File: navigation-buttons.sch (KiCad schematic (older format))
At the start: 26 parts

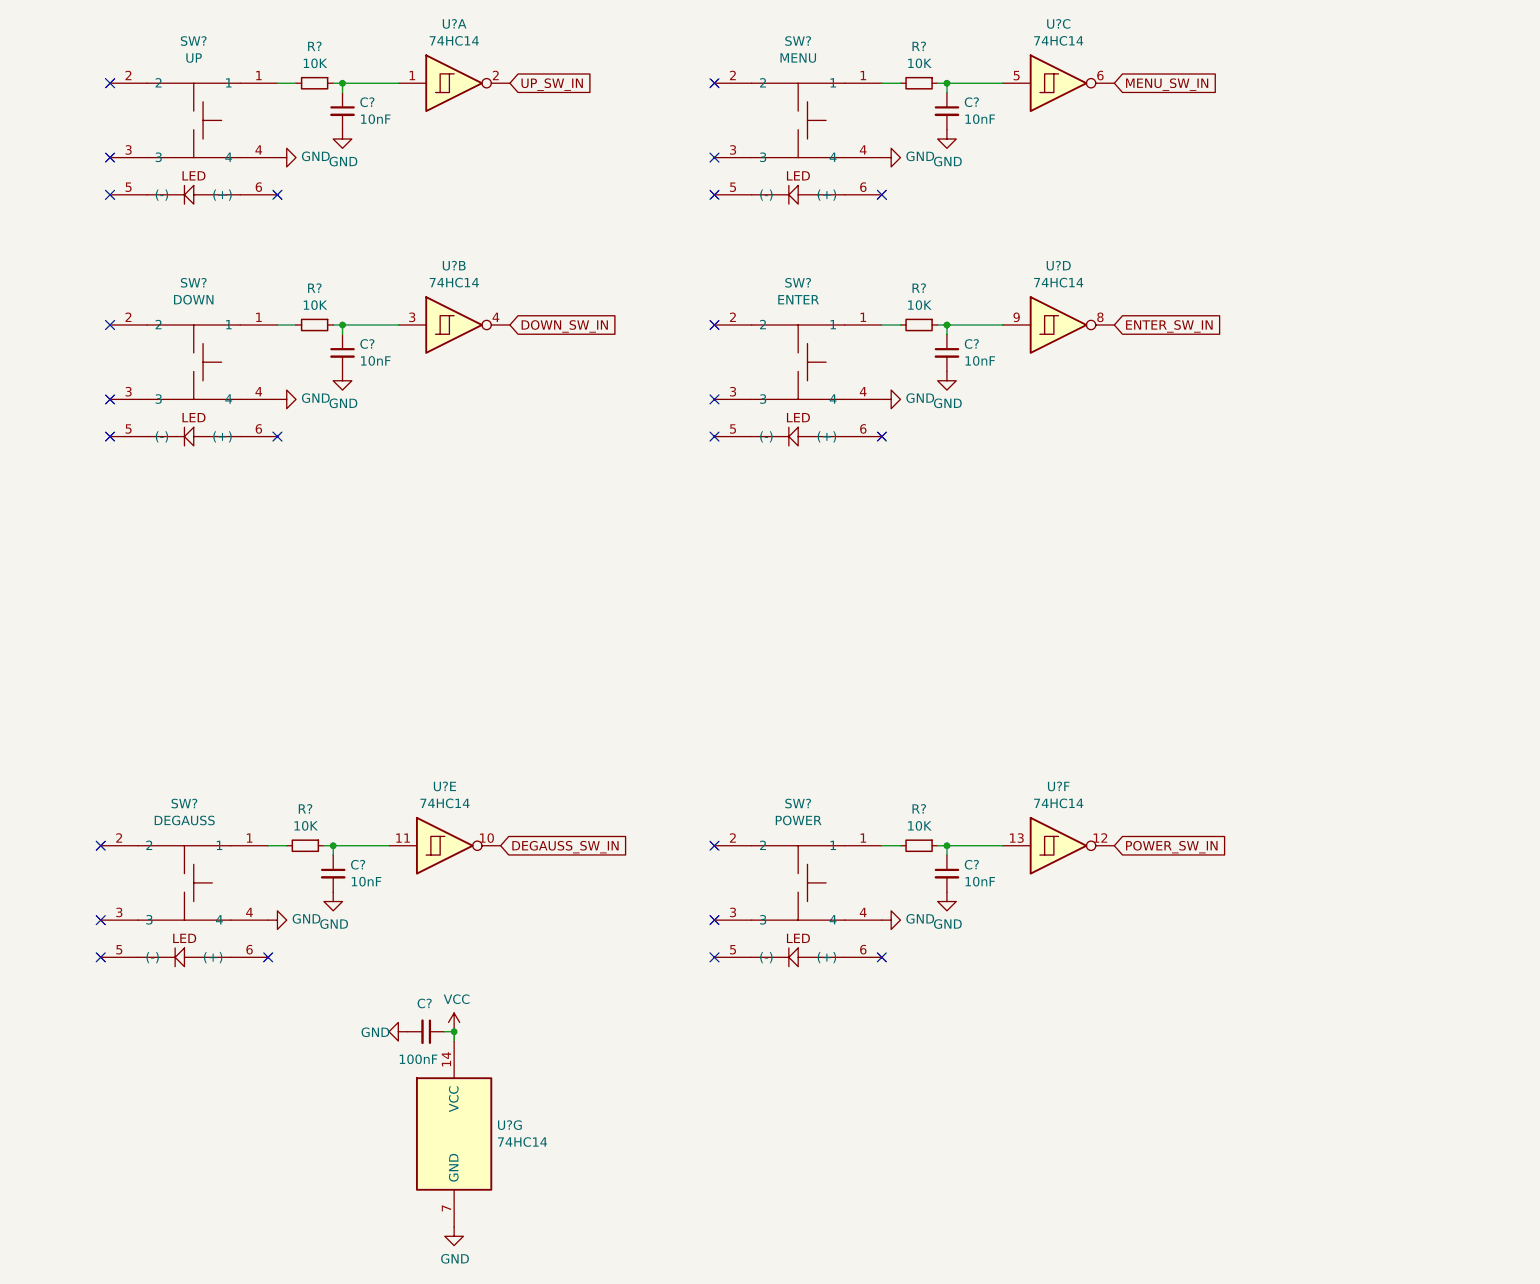
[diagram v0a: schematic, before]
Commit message: Initial PCB routed
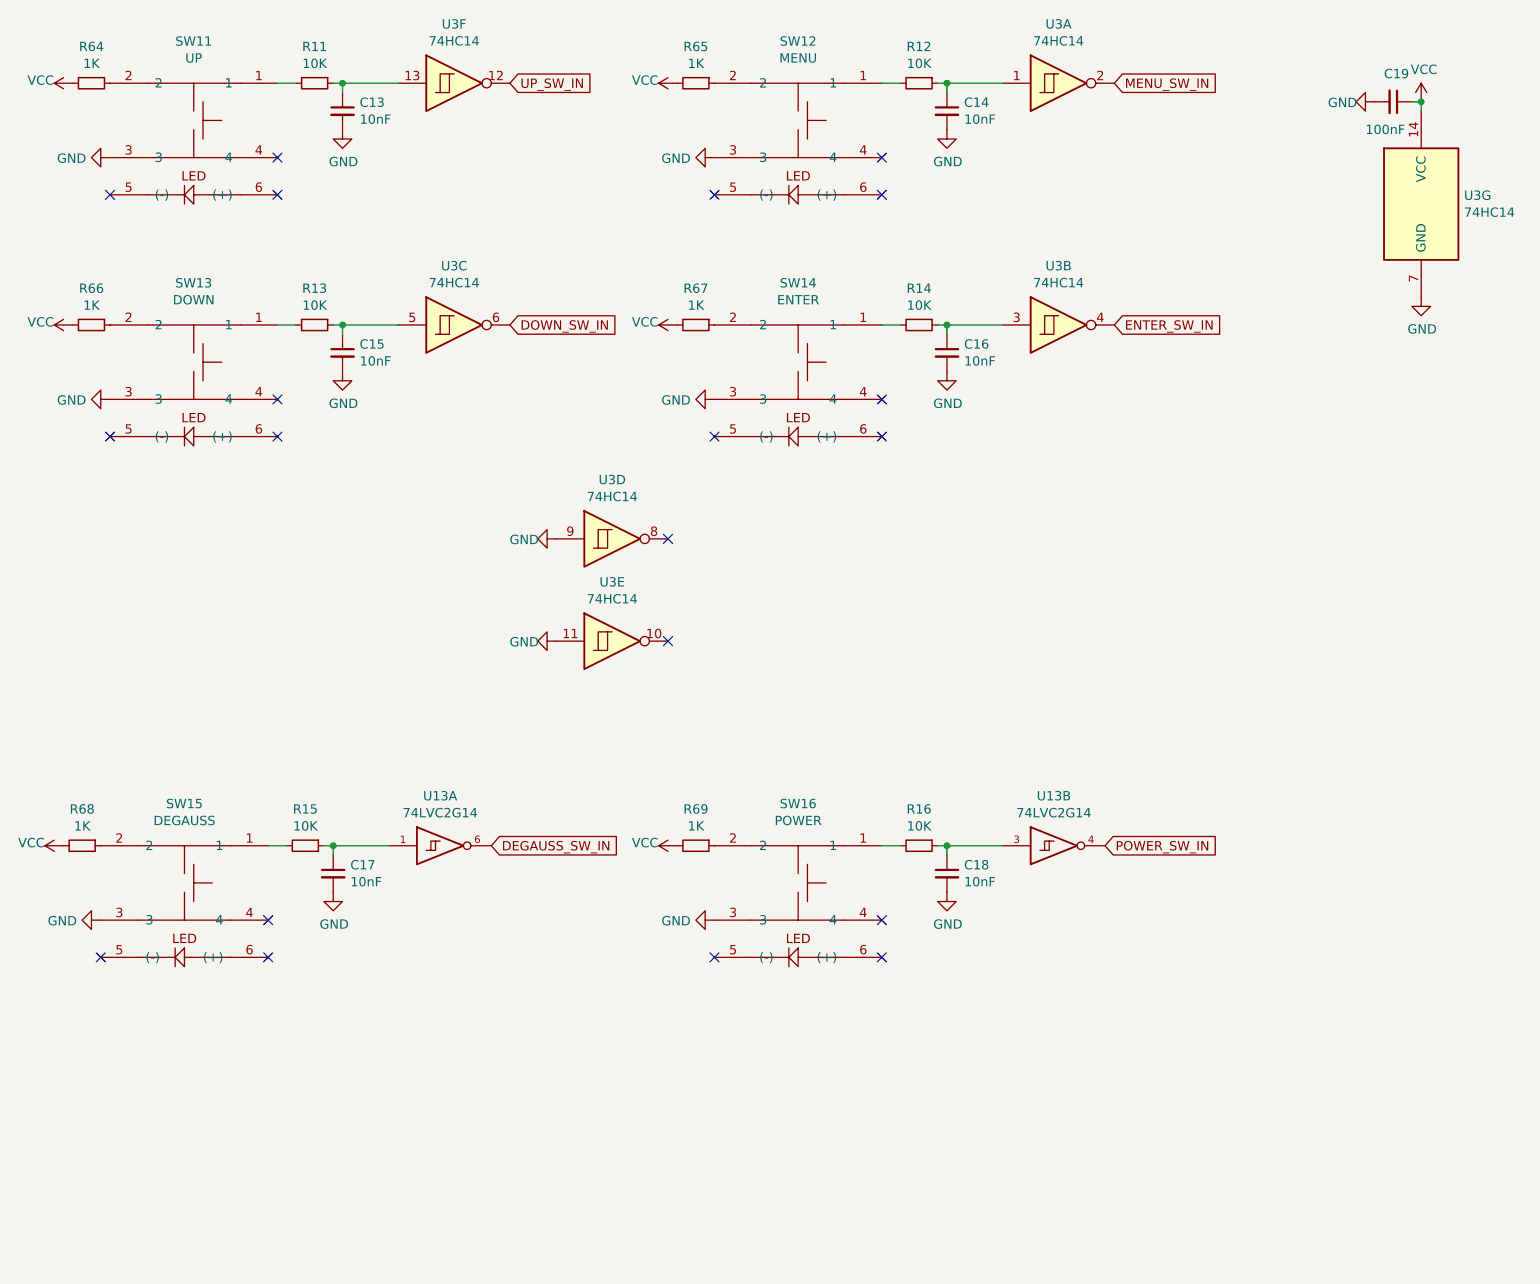
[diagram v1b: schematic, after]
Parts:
- removed U? (x2): 74HC14, symbol 74xx:74HC14
- added R64, R65, R66, R67, R68, R69: 1K, Resistor_SMD:R_0603_1608Metric_Pad0.98x0.95mm_HandSolder, symbol Device:R_Small
- added U13: 74LVC2G14, Package_TO_SOT_SMD:SOT-23-6_Handsoldering, symbol 74xGxx:74LVC2G14
- added unit 6 of U3
- added unit 5 of U3
- C13, C14, C15, C16, C17, C18, C19: renamed from C?; footprint (none) -> Capacitor_SMD:C_0603_1608Metric_Pad1.08x0.95mm_HandSolder
- R11, R12, R13, R14, R15, R16: renamed from R?; footprint (none) -> Resistor_SMD:R_0603_1608Metric_Pad0.98x0.95mm_HandSolder
- SW11, SW12, SW13, SW14, SW15, SW16: renamed from SW?; footprint (none) -> TL-1240:TL-1240
- U3: renamed from U?; footprint (none) -> Package_SO:SSOP-14_5.3x6.2mm_P0.65mm
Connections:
- net DEGAUSS_SW_IN: now also U13.6
- net DOWN_SW_IN: now also U3.6; no longer U3.4
- net ENTER_SW_IN: now also U3.4; no longer U3.8
- net GND: now also SW11.3, SW12.3, SW13.3, SW14.3, SW15.3, SW16.3, U3.9, U13.2 (GND), U13.2 (GND), U3.11; no longer SW11.4, SW12.4, SW13.4, SW14.4, SW15.4, SW16.4
- net MENU_SW_IN: now also U3.2; no longer U3.6
- net POWER_SW_IN: now also U13.4
- net UP_SW_IN: now also U3.12; no longer U3.2
- net VCC: now also R64.2, R65.2, R66.2, R67.2, R68.2, R69.2, U13.5 (VCC), U13.5 (VCC)
- net at SW11.2: now also R64.1
- net at C13.1, R11.1: now also U3.13; no longer U3.1
- net at SW13.2: now also R66.1
- net at C15.1, R13.1: now also U3.5; no longer U3.3
- net at SW12.2: now also R65.1
- net at C14.1, R12.1: now also U3.1; no longer U3.5
- net at SW14.2: now also R67.1
- net at C16.1, R14.1: now also U3.3; no longer U3.9
- net at SW15.2: now also R68.1
- net at C17.1, R15.1: now also U13.1
- net at SW16.2: now also R69.1
- net at C18.1, R16.1: now also U13.3
- no-connect marks 24 -> 20
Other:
- moved on the sheet: C19, U3A, U3B, U3C, U3D, U3G

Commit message: Initial revision B
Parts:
- SW11, SW12, SW13, SW14, SW15, SW16: footprint TL-1240:TL-1240 -> TL-1265:TL-1265_NO_LED; symbol e-switch-tact:TL-1240 -> e-switch-tact:TL-1240-NO_LED
- U3: footprint Package_SO:SSOP-14_5.3x6.2mm_P0.65mm -> Package_SO:TSSOP-14_4.4x5mm_P0.65mm
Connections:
- no-connect marks 20 -> 8
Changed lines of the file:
@@
 $EndDescr
 $Comp
-L e-switch-tact:TL-1240 SW13
+L e-switch-tact:TL-1240-NO_LED SW13
 U 1 1 61AC16B9
-P 1450 2650
-F 0 "SW13" H 1450 3125 50  0000 C CNN
-F 1 "DOWN" H 1450 3034 50  0000 C CNN
-F 2 "TL-1240:TL-1240" H 1450 2800 50  0001 C CNN
-F 3 "" H 1450 2800 50  0001 C CNN
-	1    1450 2650
-	1    0    0    -1
-$EndComp
-NoConn ~ 1000 3000
-NoConn ~ 1900 3000
+P 1450 2600
+F 0 "SW13" H 1450 3075 50  0000 C CNN
+F 1 "DOWN" H 1450 2984 50  0000 C CNN
+F 2 "TL-1265:TL-1265_NO_LED" H 1450 2750 50  0001 C CNN
+F 3 "" H 1450 2750 50  0001 C CNN
+	1    1450 2600
+	1    0    0    -1
+$EndComp
 NoConn ~ 1900 2800
 $Comp
@@
 $EndComp
 NoConn ~ 1900 1500
-NoConn ~ 1900 1700
-NoConn ~ 1000 1700
-$Comp
-L e-switch-tact:TL-1240 SW11
+$Comp
+L e-switch-tact:TL-1240-NO_LED SW11
 U 1 1 61AB54CB
-P 1450 1350
-F 0 "SW11" H 1450 1825 50  0000 C CNN
-F 1 "UP" H 1450 1734 50  0000 C CNN
-F 2 "TL-1240:TL-1240" H 1450 1500 50  0001 C CNN
-F 3 "" H 1450 1500 50  0001 C CNN
-	1    1450 1350
-	1    0    0    -1
-$EndComp
-$Comp
-L e-switch-tact:TL-1240 SW12
-U 1 1 61AC42D3
-P 4700 1350
-F 0 "SW12" H 4700 1825 50  0000 C CNN
-F 1 "MENU" H 4700 1734 50  0000 C CNN
-F 2 "TL-1240:TL-1240" H 4700 1500 50  0001 C CNN
-F 3 "" H 4700 1500 50  0001 C CNN
-	1    4700 1350
-	1    0    0    -1
-$EndComp
-NoConn ~ 4250 1700
-NoConn ~ 5150 1700
+P 1450 1300
+F 0 "SW11" H 1450 1775 50  0000 C CNN
+F 1 "UP" H 1450 1684 50  0000 C CNN
+F 2 "TL-1265:TL-1265_NO_LED" H 1450 1450 50  0001 C CNN
+F 3 "" H 1450 1450 50  0001 C CNN
+	1    1450 1300
+	1    0    0    -1
+$EndComp
 NoConn ~ 5150 1500
 $Comp
@@
 MENU_SW_IN
 $Comp
-L e-switch-tact:TL-1240 SW14
+L e-switch-tact:TL-1240-NO_LED SW14
 U 1 1 61AC5650
-P 4700 2650
-F 0 "SW14" H 4700 3125 50  0000 C CNN
-F 1 "ENTER" H 4700 3034 50  0000 C CNN
-F 2 "TL-1240:TL-1240" H 4700 2800 50  0001 C CNN
-F 3 "" H 4700 2800 50  0001 C CNN
-	1    4700 2650
-	1    0    0    -1
-$EndComp
-NoConn ~ 4250 3000
-NoConn ~ 5150 3000
+P 4700 2600
+F 0 "SW14" H 4700 3075 50  0000 C CNN
+F 1 "ENTER" H 4700 2984 50  0000 C CNN
+F 2 "TL-1265:TL-1265_NO_LED" H 4700 2750 50  0001 C CNN
+F 3 "" H 4700 2750 50  0001 C CNN
+	1    4700 2600
+	1    0    0    -1
+$EndComp
 NoConn ~ 5150 2800
 $Comp
@@
 ENTER_SW_IN
 $Comp
-L e-switch-tact:TL-1240 SW15
+L e-switch-tact:TL-1240-NO_LED SW15
 U 1 1 61ACA481
-P 1400 5450
-F 0 "SW15" H 1400 5925 50  0000 C CNN
-F 1 "DEGAUSS" H 1400 5834 50  0000 C CNN
-F 2 "TL-1240:TL-1240" H 1400 5600 50  0001 C CNN
-F 3 "" H 1400 5600 50  0001 C CNN
-	1    1400 5450
-	1    0    0    -1
-$EndComp
-NoConn ~ 950  5800
-NoConn ~ 1850 5800
+P 1400 5400
+F 0 "SW15" H 1400 5875 50  0000 C CNN
+F 1 "DEGAUSS" H 1400 5784 50  0000 C CNN
+F 2 "TL-1265:TL-1265_NO_LED" H 1400 5550 50  0001 C CNN
+F 3 "" H 1400 5550 50  0001 C CNN
+	1    1400 5400
+	1    0    0    -1
+$EndComp
 NoConn ~ 1850 5600
 $Comp
@@
 DEGAUSS_SW_IN
 $Comp
-L e-switch-tact:TL-1240 SW16
+L e-switch-tact:TL-1240-NO_LED SW16
 U 1 1 61AD8CF5
-P 4700 5450
-F 0 "SW16" H 4700 5925 50  0000 C CNN
-F 1 "POWER" H 4700 5834 50  0000 C CNN
-F 2 "TL-1240:TL-1240" H 4700 5600 50  0001 C CNN
-F 3 "" H 4700 5600 50  0001 C CNN
-	1    4700 5450
-	1    0    0    -1
-$EndComp
-NoConn ~ 4250 5800
-NoConn ~ 5150 5800
+P 4700 5400
+F 0 "SW16" H 4700 5875 50  0000 C CNN
+F 1 "POWER" H 4700 5784 50  0000 C CNN
+F 2 "TL-1265:TL-1265_NO_LED" H 4700 5550 50  0001 C CNN
+F 3 "" H 4700 5550 50  0001 C CNN
+	1    4700 5400
+	1    0    0    -1
+$EndComp
 NoConn ~ 5150 5600
 $Comp
@@
 F 0 "U3" H 6100 1417 50  0000 C CNN
 F 1 "74HC14" H 6100 1326 50  0000 C CNN
-F 2 "Package_SO:SSOP-14_5.3x6.2mm_P0.65mm" H 6100 1100 50  0001 C CNN
+F 2 "Package_SO:TSSOP-14_4.4x5mm_P0.65mm" H 6100 1100 50  0001 C CNN
 F 3 "http://www.ti.com/lit/gpn/sn74HC14" H 6100 1100 50  0001 C CNN
 	1    6100 1100
@@
 F 0 "U3" H 6100 2717 50  0000 C CNN
 F 1 "74HC14" H 6100 2626 50  0000 C CNN
-F 2 "Package_SO:SSOP-14_5.3x6.2mm_P0.65mm" H 6100 2400 50  0001 C CNN
+F 2 "Package_SO:TSSOP-14_4.4x5mm_P0.65mm" H 6100 2400 50  0001 C CNN
 F 3 "http://www.ti.com/lit/gpn/sn74HC14" H 6100 2400 50  0001 C CNN
 	2    6100 2400
@@
 F 0 "U3" H 3700 3867 50  0000 C CNN
 F 1 "74HC14" H 3700 3776 50  0000 C CNN
-F 2 "Package_SO:SSOP-14_5.3x6.2mm_P0.65mm" H 3700 3550 50  0001 C CNN
+F 2 "Package_SO:TSSOP-14_4.4x5mm_P0.65mm" H 3700 3550 50  0001 C CNN
 F 3 "http://www.ti.com/lit/gpn/sn74HC14" H 3700 3550 50  0001 C CNN
 	4    3700 3550
@@
 F 0 "U3" H 2850 2717 50  0000 C CNN
 F 1 "74HC14" H 2850 2626 50  0000 C CNN
-F 2 "Package_SO:SSOP-14_5.3x6.2mm_P0.65mm" H 2850 2400 50  0001 C CNN
+F 2 "Package_SO:TSSOP-14_4.4x5mm_P0.65mm" H 2850 2400 50  0001 C CNN
 F 3 "http://www.ti.com/lit/gpn/sn74HC14" H 2850 2400 50  0001 C CNN
 	3    2850 2400
@@
 F 0 "U3" H 8280 1796 50  0000 L CNN
 F 1 "74HC14" H 8280 1705 50  0000 L CNN
-F 2 "Package_SO:SSOP-14_5.3x6.2mm_P0.65mm" H 8050 1750 50  0001 C CNN
+F 2 "Package_SO:TSSOP-14_4.4x5mm_P0.65mm" H 8050 1750 50  0001 C CNN
 F 3 "http://www.ti.com/lit/gpn/sn74HC14" H 8050 1750 50  0001 C CNN
 	7    8050 1750
@@
 F 0 "U3" H 2850 1417 50  0000 C CNN
 F 1 "74HC14" H 2850 1326 50  0000 C CNN
-F 2 "Package_SO:SSOP-14_5.3x6.2mm_P0.65mm" H 2850 1100 50  0001 C CNN
+F 2 "Package_SO:TSSOP-14_4.4x5mm_P0.65mm" H 2850 1100 50  0001 C CNN
 F 3 "http://www.ti.com/lit/gpn/sn74HC14" H 2850 1100 50  0001 C CNN
 	6    2850 1100
@@
 F 0 "U3" H 3700 4417 50  0000 C CNN
 F 1 "74HC14" H 3700 4326 50  0000 C CNN
-F 2 "Package_SO:SSOP-14_5.3x6.2mm_P0.65mm" H 3700 4100 50  0001 C CNN
+F 2 "Package_SO:TSSOP-14_4.4x5mm_P0.65mm" H 3700 4100 50  0001 C CNN
 F 3 "http://www.ti.com/lit/gpn/sn74HC14" H 3700 4100 50  0001 C CNN
 	5    3700 4100
@@
 	0    -1   -1   0
 $EndComp
+$Comp
+L e-switch-tact:TL-1240-NO_LED SW12
+U 1 1 61AC42D3
+P 4700 1300
+F 0 "SW12" H 4700 1775 50  0000 C CNN
+F 1 "MENU" H 4700 1684 50  0000 C CNN
+F 2 "TL-1265:TL-1265_NO_LED" H 4700 1450 50  0001 C CNN
+F 3 "" H 4700 1450 50  0001 C CNN
+	1    4700 1300
+	1    0    0    -1
+$EndComp
 $EndSCHEMATC
